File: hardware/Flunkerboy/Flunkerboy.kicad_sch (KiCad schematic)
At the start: 29 parts, among them J1 GameBoy_GamePak_DMG-09, J2 Conn_01x01_Socket, J3 Conn_01x01_Socket, Q1 AO3400A, Q2 AO3400A, Q3 AO3400A, Q4 AO3400A, Q5 AO3400A, Q6 AO3400A, U1 74LS574, U2 74LS04, U5 AD9283, U6 OPA2333AIDR(UMW), U7 CD4051B

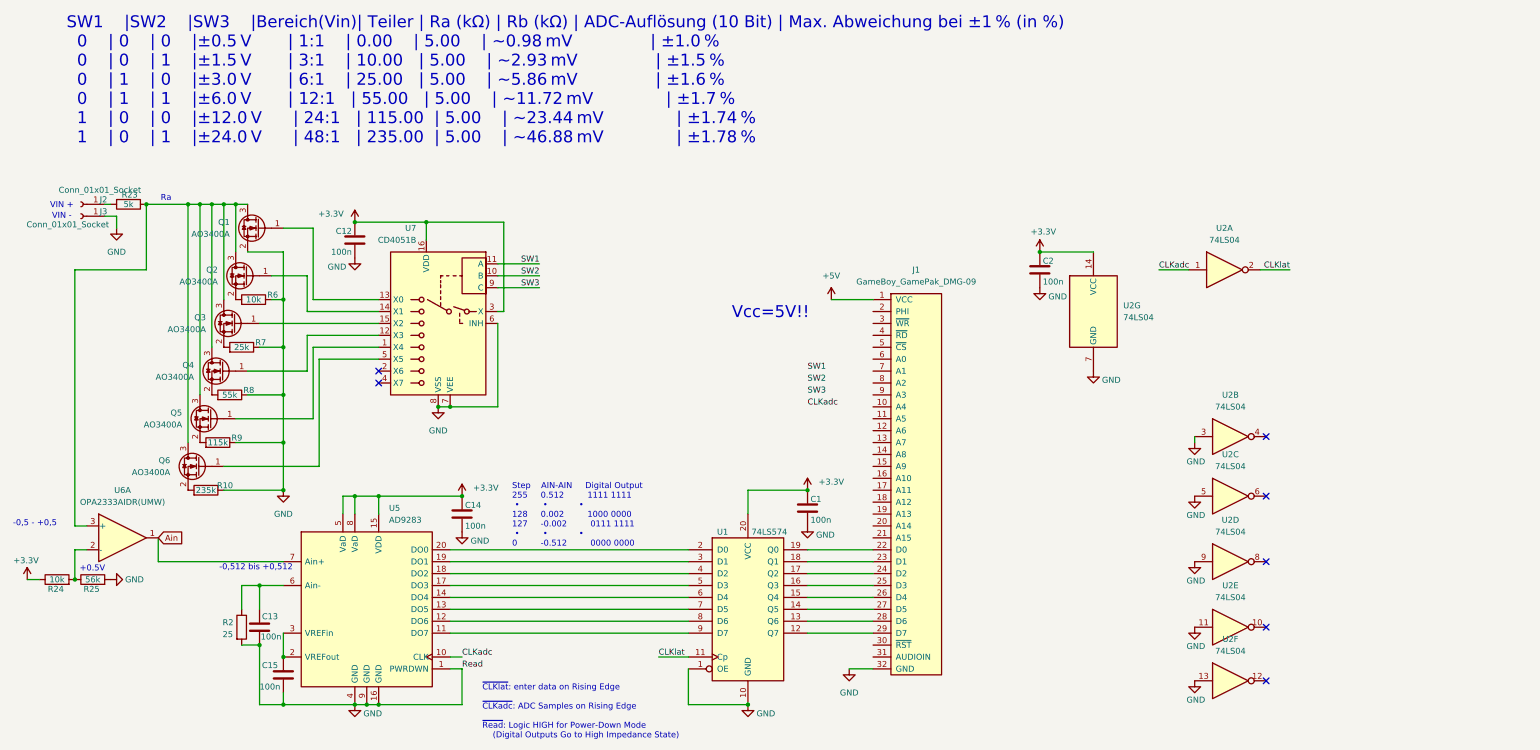
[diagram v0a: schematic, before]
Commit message: add mosfets
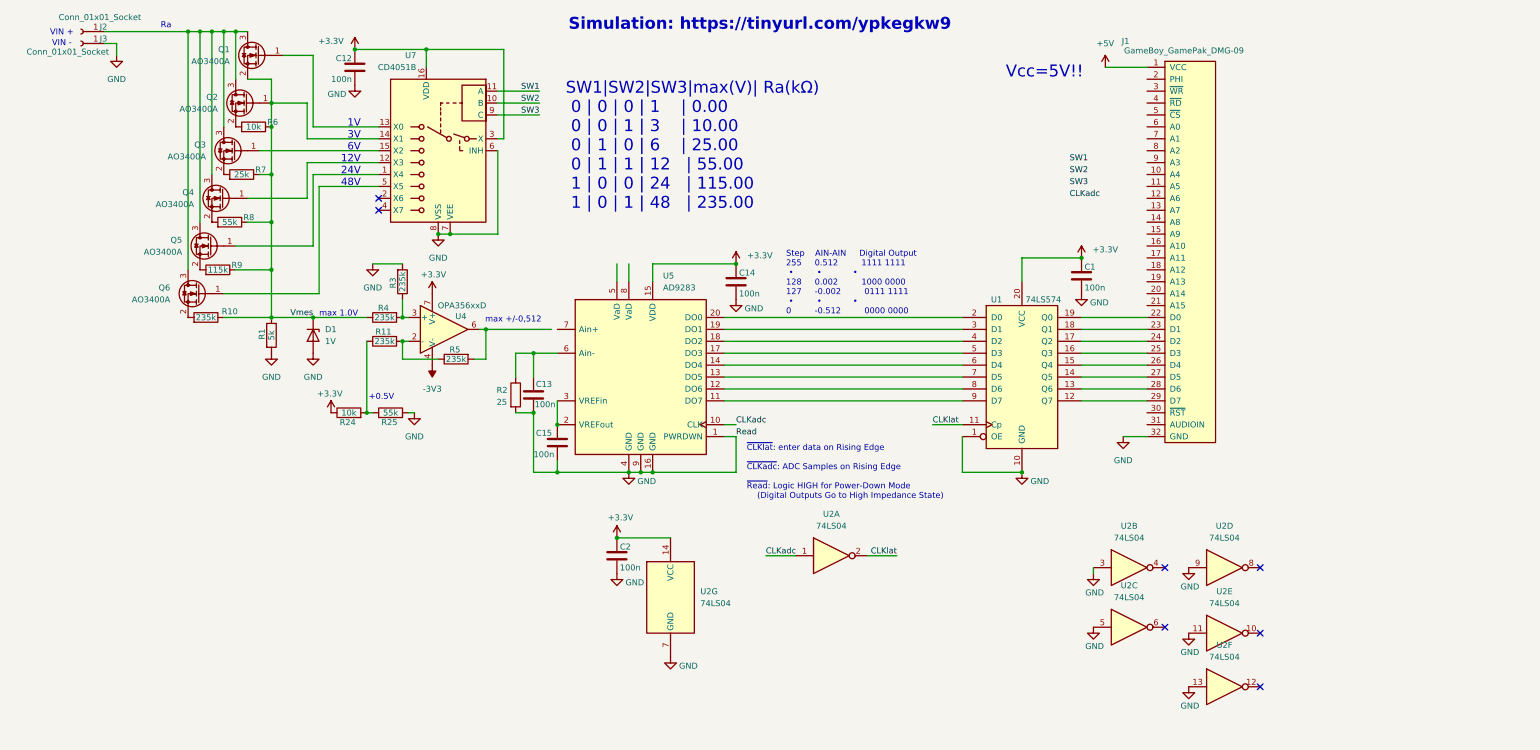
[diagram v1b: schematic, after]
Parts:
- removed U6: OPA2333AIDR(UMW), Package_SO:SO-8_3.9x4.9mm_P1.27mm, symbol Amplifier_Operational:OPA2333xxD
- added D1: 1V, symbol Device:D_Zener
- added R11, R3, R4, R5: 235k, Resistor_SMD:R_0805_2012Metric_Pad1.20x1.40mm_HandSolder, symbol Device:R
- added U4: OPA356xxD, Package_SO:SOIC-8_3.9x4.9mm_P1.27mm, symbol Amplifier_Operational:OPA356xxD
- R25: value 56k -> 55k
- renumbered R23 to R1
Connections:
- net +3.3V: now also U4.7 (V+); no longer U5.5 (VaD), U5.8 (VaD)
- net GND: now also R1.2, D1.2 (A), R3.2; no longer Q1.2 (S), R10.1, R6.1, R7.1, R8.1, R9.1
- net Vmes: now reaches Q2.1 (G), U7.14 (X1)
- net Vmes: now also Q1.2 (S), R1.1, R10.1, R6.1, R7.1, R8.1, R9.1, D1.1 (K), R4.1
- net at R24.2, R25.1: now also R11.1
- net at J2.1 (Pin_1): now also Q1.3 (D), Q2.3 (D), Q3.3 (D), Q4.3 (D), Q5.3 (D), Q6.3 (D); no longer R1.2
- net Ain: no longer names the net of U5.7 (Ain+)
- new net: R11.2, R5.1, U4.2 (-)
- new net: R3.1, R4.2, U4.3 (+)
- new net: R5.2, U4.6
- new net -3V3: U4.4 (V-)
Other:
- note added: "1V 3V 6V 12V 24V 48V"
- note added: "SW1|SW2|SW3|max(V)| Ra(kΩ) 0 | 0 | 0 | 1 | 0.00 0 | 0 | 1 | 3 | 10.00 0 | 1 | 0 | 6 | 25.00 0 | 1 | 1 | 12 | 55.00 1 | 0 | 0 | 24 | 115.00 1 | 0 | 1 | 48 | 235.00"
- note added: "Simulation: https://tinyurl.com/ypkegkw9"
- note added: "max +/-0,512"
- note added: "max 1.0V"
- note removed: "-0,5 - +0,5"
- note removed: "-0,512 bis +0,512"
- note removed: "SW1 |SW2 |SW3 |Bereich(Vin)| Teiler | Ra (kΩ) | Rb (kΩ) | ADC-Auflösung (10 Bit) | Max. Abweichung bei ±1 % (in %) 0 | 0 | 0 |±0.5 V | 1:1 | 0.00 | 5.00 | ~0.98 mV | ±1.0 % 0 | 0 | 1 |±1.5 V | 3:1 | 10.00 | 5.00 | ~2.93 mV | ±1.5 % 0 | 1 | 0 |±3.0 V | 6:1 | 25.00 | 5.00 | ~5.86 mV | ±1.6 % 0 | 1 | 1 |±6.0 V | 12:1 | 55.00 | 5.00 | ~11.72 mV | ±1.7 % 1 | 0 | 0 |±12.0 V | 24:1 | 115.00 | 5.00 | ~23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"
- moved on the sheet: C1, C12, C13, C14, C15, C2, J1, J2, J3, Q1, Q2, Q3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

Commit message: build imput devider
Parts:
- removed C12, C2: 100n, Capacitor_SMD:C_0603_1608Metric, symbol Device:C
- removed J2, J3: Conn_01x01_Socket, Connector:Banana_Cliff_FCR7350B_S16N-PC_Horizontal, symbol Connector:Conn_01x01_Socket
- removed Q1, Q2, Q3, Q4, Q5, Q6: AO3400A, Package_TO_SOT_SMD:SOT-23, symbol Transistor_FET:AO3400A
- removed R1: 5k, Resistor_SMD:R_0805_2012Metric_Pad1.20x1.40mm_HandSolder, symbol Device:R
- removed R10: 235k, Resistor_SMD:R_0805_2012Metric_Pad1.20x1.40mm_HandSolder, symbol Device:R
- removed R6: 10k, Resistor_SMD:R_0805_2012Metric_Pad1.20x1.40mm_HandSolder, symbol Device:R
- removed R7: 25k, Resistor_SMD:R_0805_2012Metric_Pad1.20x1.40mm_HandSolder, symbol Device:R
- removed R8: 55k, Resistor_SMD:R_0805_2012Metric_Pad1.20x1.40mm_HandSolder, symbol Device:R
- removed R9: 115k, Resistor_SMD:R_0805_2012Metric_Pad1.20x1.40mm_HandSolder, symbol Device:R
- removed U2: 74LS04, Package_SO:SO-14_5.3x10.2mm_P1.27mm, symbol 74xx:74LS04
- removed U7: CD4051B, Package_SO:SO-16_3.9x9.9mm_P1.27mm, symbol Analog_Switch:CD4051B
- D4: renamed from D1; footprint (none) -> Diode_SMD:D_SOD-123F
- renumbered R4 to R10, R3 to R12, R5 to R13, R2 to R14, U4 to U1, U5 to U13, U1 to U14
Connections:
- no-connect marks 7 -> 0
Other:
- added sheet Eingangsteiler (eingangsteiler.kicad_sch)
- note removed: "1V 3V 6V 12V 24V 48V"
- note removed: "Ra"
- note removed: "SW1|SW2|SW3|max(V)| Ra(kΩ) 0 | 0 | 0 | 1 | 0.00 0 | 0 | 1 | 3 | 10.00 0 | 1 | 0 | 6 | 25.00 0 | 1 | 1 | 12 | 55.00 1 | 0 | 0 | 24 | 115.00 1 | 0 | 1 | 48 | 235.00"
- note removed: "Simulation: https://tinyurl.com/ypkegkw9"
- note removed: "VIN +"
- note removed: "VIN -"
- note removed: "max 1.0V"

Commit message: add docs
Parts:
- C1, C13, C14, C15: LCSC C69335 -> (none); LCSC part (none) -> C69335
- U13: LCSC C653448 -> (none); LCSC part (none) -> C653448
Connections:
- net at U13.7 (Ain+): now also R13.2, U1.6
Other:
- added sheet DMM 6010 (DMM_6010.kicad_sch)
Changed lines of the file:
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@@
 	(wire
 		(pts
-			(xy 114.3 83.82) (xy 128.27 83.82)
+			(xy 114.3 83.82) (xy 129.54 83.82)
 		)
 		(stroke
@@
 			)
 		)
-		(property "LCSC" "C653448"
+		(property "LCSC" ""
+			(at 147.32 93.98 0)
+			(effects
+				(font
+					(size 1.27 1.27)
+				)
+				(hide yes)
+			)
+		)
+		(property "LCSC part" "C653448"
 			(at 147.32 93.98 0)
 			(effects
@@
 			)
 		)
-		(property "LCSC" "C69335"
+		(property "LCSC" ""
 			(at 241.3 72.39 0)
 			(effects
@@
 			)
 		)
+		(property "LCSC part" "C69335"
+			(at 241.3 72.39 0)
+			(effects
+				(font
+					(size 1.27 1.27)
+				)
+				(hide yes)
+			)
+		)
 		(pin "1"
 		)
@@
 			)
 		)
-		(property "LCSC" "C69335"
+		(property "LCSC" ""
 			(at 129.54 107.95 0)
 			(effects
@@
 		)
 		(property "SOURCED" "ok"
+			(at 129.54 107.95 0)
+			(effects
+				(font
+					(size 1.27 1.27)
+				)
+				(hide yes)
+			)
+		)
+		(property "LCSC part" "C69335"
 			(at 129.54 107.95 0)
 			(effects
@@
 			)
 		)
-		(property "LCSC" "C69335"
+		(property "LCSC" ""
 			(at 167.64 73.66 0)
 			(effects
@@
 			)
 		)
+		(property "LCSC part" "C69335"
+			(at 167.64 73.66 0)
+			(effects
+				(font
+					(size 1.27 1.27)
+				)
+				(hide yes)
+			)
+		)
 		(pin "1"
 		)
@@
 			)
 		)
-		(property "LCSC" "C69335"
+		(property "LCSC" ""
 			(at 124.46 97.79 0)
 			(effects
@@
 			)
 		)
+		(property "LCSC part" "C69335"
+			(at 124.46 97.79 0)
+			(effects
+				(font
+					(size 1.27 1.27)
+				)
+				(hide yes)
+			)
+		)
 		(pin "1"
 		)
@@
 				)
 			)
+		)
+	)
+	(sheet
+		(at 96.52 27.94)
+		(size 35.56 20.32)
+		(exclude_from_sim no)
+		(in_bom yes)
+		(on_board yes)
+		(dnp no)
+		(fields_autoplaced yes)
+		(stroke
+			(width 0.1524)
+			(type solid)
+		)
+		(fill
+			(color 0 0 0 0.0000)
+		)
+		(property "Sheetname" "DMM 6010"
+			(at 96.52 27.2284 0)
+			(effects
+				(font
+					(size 1.27 1.27)
+				)
+				(justify left bottom)
+			)
+		)
+		(property "Sheetfile" "DMM_6010.kicad_sch"
+			(at 96.52 48.8446 0)
+			(effects
+				(font
+					(size 1.27 1.27)
+				)
+				(justify left top)
+			)
+		)
+		(instances
+			(project "Flunkerboy"
+				(path "/560f5fb2-d2ab-4954-a8f4-77a42c998ddb"
+					(page "3")
+				)
+			)
